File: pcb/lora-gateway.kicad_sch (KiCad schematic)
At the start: 22 parts, among them J1 USB_B_Micro, J2 Conn_01x06, J3 Conn_01x06, J4 Conn_Coaxial, J5 AVR-JTAG-10, J6 AVR-ISP-6, SW1 SW_Push, U1 RFM95W-868S2, U2 ATmega2560-16A, U3 LM1117-3.3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

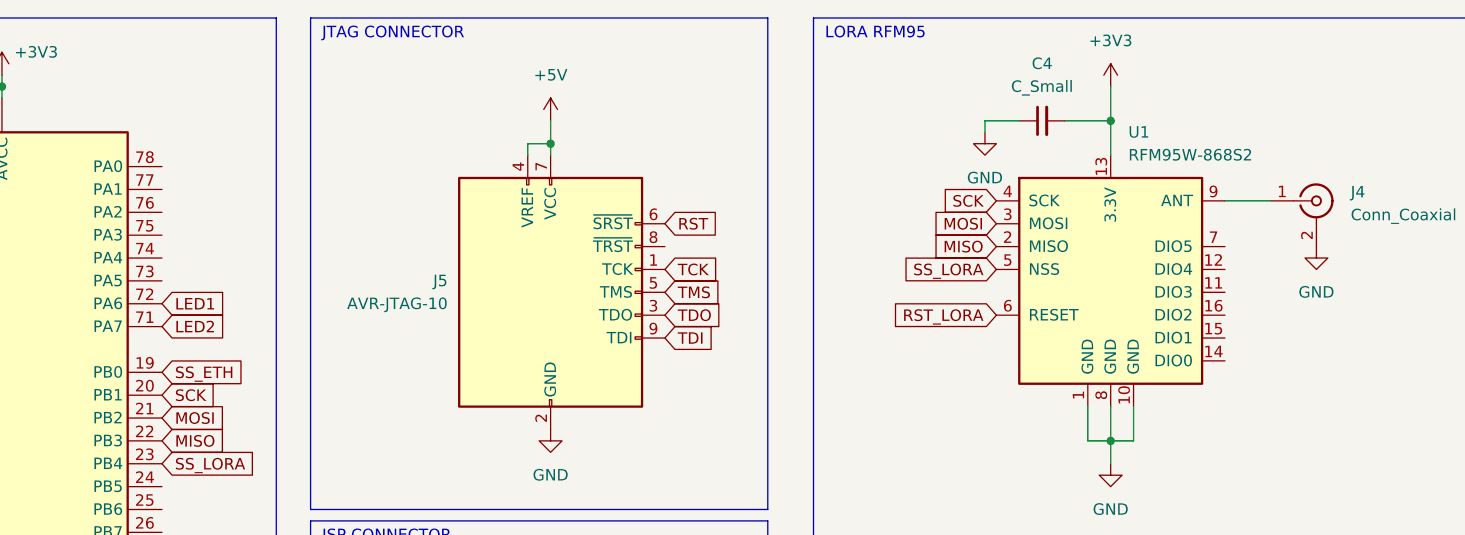
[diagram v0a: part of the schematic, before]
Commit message: add rfm95 wiring
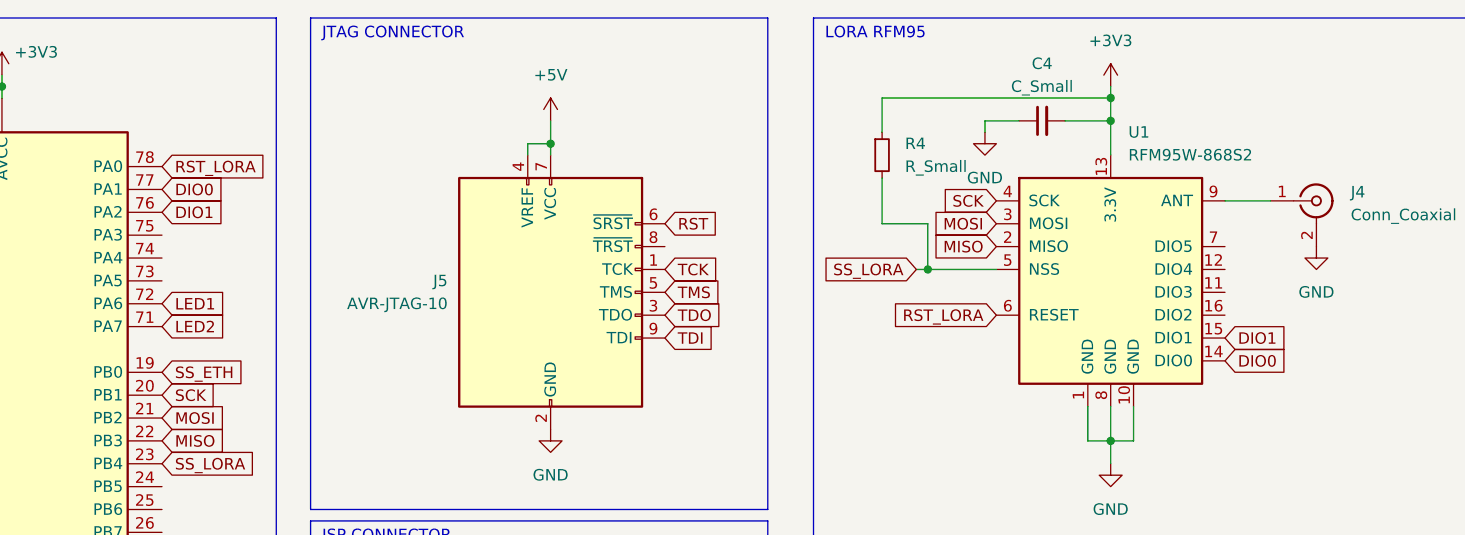
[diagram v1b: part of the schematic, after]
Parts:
- added R4: R_Small, Resistor_SMD:R_0603_1608Metric, symbol Device:R_Small
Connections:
- net +3V3: now also R4.1
- net RST_LORA: now also U2.78 (PA0)
- net SS_LORA: now also R4.2
- net DIO1: now reaches U2.76 (PA2)
- net DIO1: now also U1.15 (DIO1)
- net DIO0: now reaches U2.77 (PA1)
- net DIO0: now also U1.14 (DIO0)
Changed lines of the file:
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@@
   (junction (at 41.91 74.93) (diameter 0) (color 0 0 0 0)
   )
+  (junction (at 199.39 43.18) (diameter 0) (color 0 0 0 0)
+  )
   (junction (at 219.71 26.67) (diameter 0) (color 0 0 0 0)
   )
@@
   (junction (at 45.72 36.83) (diameter 0) (color 0 0 0 0)
   )
+  (junction (at 219.71 24.13) (diameter 0) (color 0 0 0 0)
+  )
   (junction (at 66.04 44.45) (diameter 0) (color 0 0 0 0)
   )
@@
     (stroke (width 0) (type default))
   )
+  (wire (pts (xy 194.31 33.02) (xy 194.31 38.1))
+    (stroke (width 0) (type default))
+  )
   (wire (pts (xy 219.71 96.52) (xy 220.98 96.52))
     (stroke (width 0) (type default))
@@
     (stroke (width 0) (type default))
   )
+  (wire (pts (xy 194.31 24.13) (xy 219.71 24.13))
+    (stroke (width 0) (type default))
+  )
   (wire (pts (xy 219.71 62.23) (xy 219.71 64.77))
     (stroke (width 0) (type default))
@@
     (stroke (width 0) (type default))
   )
+  (wire (pts (xy 194.31 27.94) (xy 194.31 24.13))
+    (stroke (width 0) (type default))
+  )
   (polyline (pts (xy 67.31 52.07) (xy 67.31 182.88))
     (stroke (width 0) (type default))
@@
     (stroke (width 0) (type default))
   )
+  (wire (pts (xy 219.71 24.13) (xy 219.71 26.67))
+    (stroke (width 0) (type default))
+  )
   (wire (pts (xy 219.71 58.42) (xy 219.71 62.23))
     (stroke (width 0) (type default))
@@
     (stroke (width 0) (type default))
   )
+  (wire (pts (xy 199.39 43.18) (xy 207.01 43.18))
+    (stroke (width 0) (type default))
+  )
   (wire (pts (xy 71.12 31.75) (xy 73.66 31.75))
     (stroke (width 0) (type default))
@@
     (stroke (width 0) (type default))
   )
+  (wire (pts (xy 199.39 38.1) (xy 199.39 43.18))
+    (stroke (width 0) (type default))
+  )
   (wire (pts (xy 46.99 74.93) (xy 41.91 74.93))
     (stroke (width 0) (type default))
@@
     (stroke (width 0) (type default))
   )
+  (wire (pts (xy 194.31 38.1) (xy 199.39 38.1))
+    (stroke (width 0) (type default))
+  )
   (polyline (pts (xy 15.24 52.07) (xy 40.64 52.07))
     (stroke (width 0) (type default))
@@
     (stroke (width 0) (type default))
   )
-  (wire (pts (xy 219.71 22.86) (xy 219.71 26.67))
+  (wire (pts (xy 219.71 22.86) (xy 219.71 24.13))
     (stroke (width 0) (type default))
   )
@@
   )
   (polyline (pts (xy 181.61 15.24) (xy 130.81 15.24))
+    (stroke (width 0) (type default))
+  )
+  (wire (pts (xy 198.12 43.18) (xy 199.39 43.18))
     (stroke (width 0) (type default))
   )
@@
   (text "JTAG CONNECTOR" (at 132.08 17.78 0)
     (effects (font (size 1.27 1.27)) (justify left bottom))
+  )
+  (global_label "DIO0" (shape input) (at 114.3 34.29 0) (fields_autoplaced)
+    (effects (font (size 1.27 1.27)) (justify left))
+    (property "Intersheetrefs" "${INTERSHEET_REFS}" (at 121.7 34.29 0)
+      (effects (font (size 1.27 1.27)) (justify left) hide)
+    )
   )
   (global_label "RST_LORA" (shape input) (at 207.01 48.26 180) (fields_autoplaced)
@@
     )
   )
+  (global_label "DIO1" (shape input) (at 114.3 36.83 0) (fields_autoplaced)
+    (effects (font (size 1.27 1.27)) (justify left))
+    (property "Intersheetrefs" "${INTERSHEET_REFS}" (at 121.7 36.83 0)
+      (effects (font (size 1.27 1.27)) (justify left) hide)
+    )
+  )
   (global_label "TMS" (shape input) (at 170.18 45.72 0) (fields_autoplaced)
     (effects (font (size 1.27 1.27)) (justify left))
@@
     (effects (font (size 1.27 1.27)) (justify left))
     (property "Intersheetrefs" "${INTERSHEET_REFS}" (at 178.1847 92.71 0)
+      (effects (font (size 1.27 1.27)) (justify left) hide)
+    )
+  )
+  (global_label "DIO1" (shape input) (at 232.41 50.8 0) (fields_autoplaced)
+    (effects (font (size 1.27 1.27)) (justify left))
+    (property "Intersheetrefs" "${INTERSHEET_REFS}" (at 239.81 50.8 0)
+      (effects (font (size 1.27 1.27)) (justify left) hide)
+    )
+  )
+  (global_label "RST_LORA" (shape input) (at 114.3 31.75 0) (fields_autoplaced)
+    (effects (font (size 1.27 1.27)) (justify left))
+    (property "Intersheetrefs" "${INTERSHEET_REFS}" (at 126.4171 31.75 0)
       (effects (font (size 1.27 1.27)) (justify left) hide)
     )
@@
     )
   )
-  (global_label "SS_LORA" (shape input) (at 207.01 43.18 180) (fields_autoplaced)
+  (global_label "SS_LORA" (shape input) (at 198.12 43.18 180) (fields_autoplaced)
     (effects (font (size 1.27 1.27)) (justify right))
-    (property "Intersheetrefs" "${INTERSHEET_REFS}" (at 195.921 43.18 0)
+    (property "Intersheetrefs" "${INTERSHEET_REFS}" (at 187.031 43.18 0)
       (effects (font (size 1.27 1.27)) (justify right) hide)
     )
@@
     (property "Intersheetrefs" "${INTERSHEET_REFS}" (at 213.8219 106.68 0)
       (effects (font (size 1.27 1.27)) (justify right) hide)
+    )
+  )
+  (global_label "DIO0" (shape input) (at 232.41 53.34 0) (fields_autoplaced)
+    (effects (font (size 1.27 1.27)) (justify left))
+    (property "Intersheetrefs" "${INTERSHEET_REFS}" (at 239.81 53.34 0)
+      (effects (font (size 1.27 1.27)) (justify left) hide)
     )
   )
@@
         )
       )
+    )
+  )
+  (symbol (lib_id "Device:R_Small") (at 194.31 30.48 0) (unit 1)
+    (in_bom yes) (on_board yes) (dnp no) (fields_autoplaced)
+    (property "Reference" "R4" (at 196.85 29.21 0)
+      (effects (font (size 1.27 1.27)) (justify left))
+    )
+    (property "Value" "R_Small" (at 196.85 31.75 0)
+      (effects (font (size 1.27 1.27)) (justify left))
+    )
+    (property "Footprint" "Resistor_SMD:R_0603_1608Metric" (at 194.31 30.48 0)
+      (effects (font (size 1.27 1.27)) hide)
+    )
+    (property "Datasheet" "~" (at 194.31 30.48 0)
+      (effects (font (size 1.27 1.27)) hide)
+    )
+    (pin "1")
+    (pin "2")
+    (instances
+      (project "lora-gateway"
+        (path "/5fd0eb65-7f10-4bbb-b642-b528dcb1ea0e"
+          (reference "R4") (unit 1)
+        )
+      )

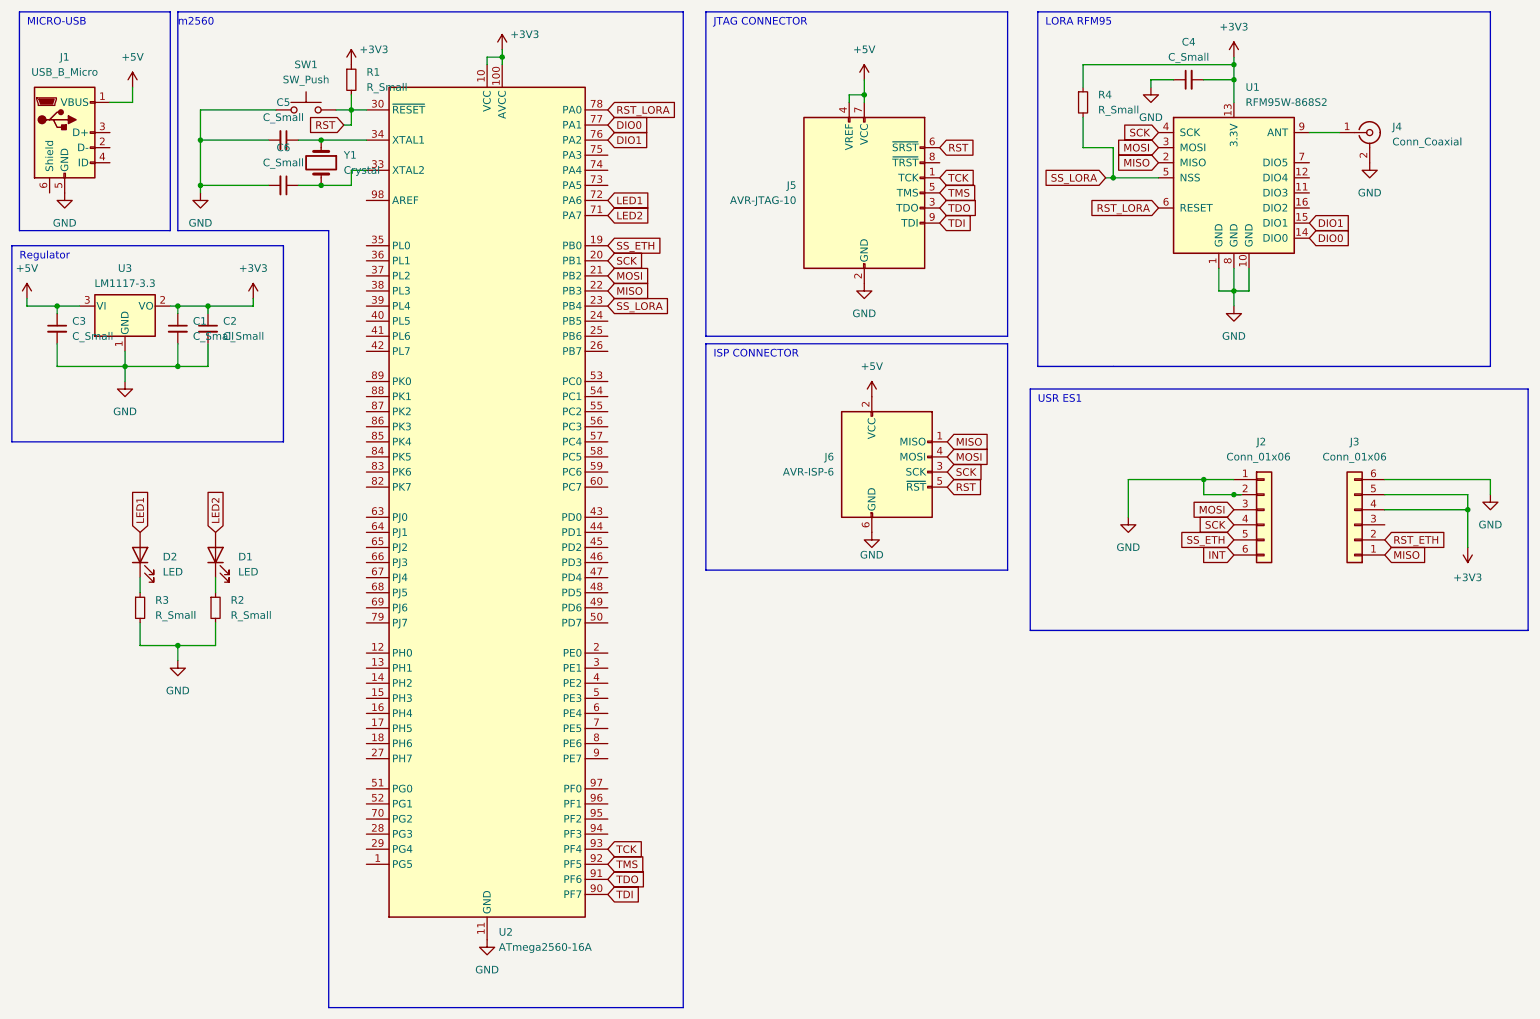
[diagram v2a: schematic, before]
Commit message: change DIO0 & DIO1 to interrupt pin
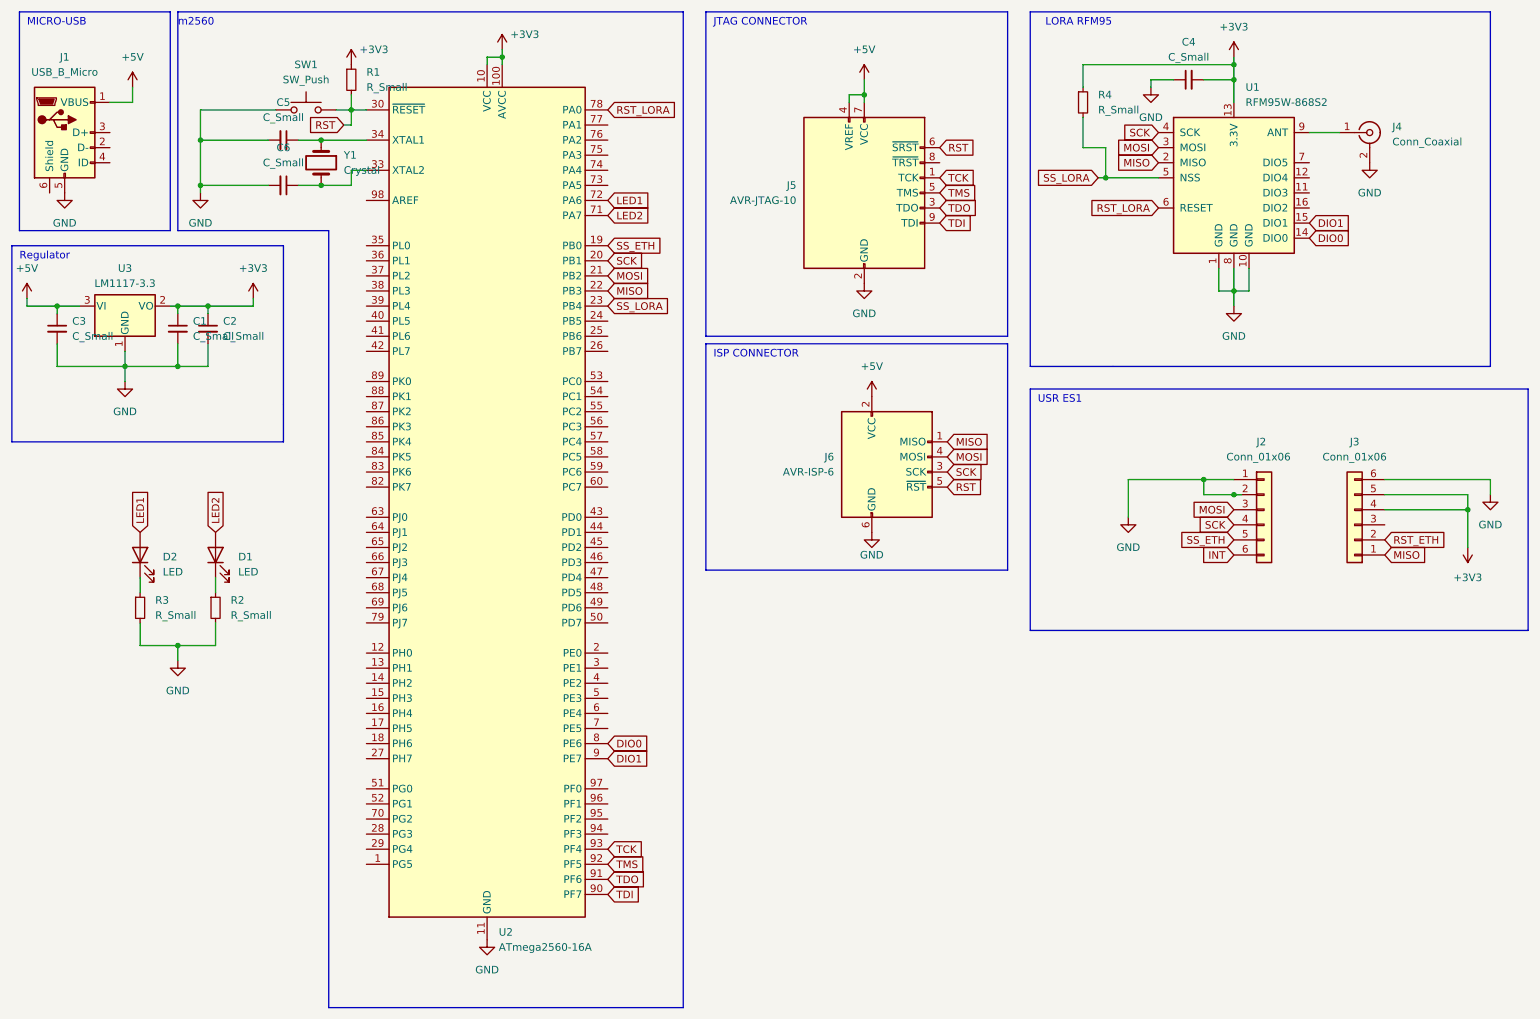
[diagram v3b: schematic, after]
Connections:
- net DIO0: now also U2.8 (PE6); no longer U2.77 (PA1)
- net DIO1: now also U2.9 (PE7); no longer U2.76 (PA2)
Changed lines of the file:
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@@
   (junction (at 41.91 74.93) (diameter 0) (color 0 0 0 0)
   )
-  (junction (at 199.39 43.18) (diameter 0) (color 0 0 0 0)
-  )
   (junction (at 219.71 26.67) (diameter 0) (color 0 0 0 0)
   )
@@
   (junction (at 96.52 22.86) (diameter 0) (color 0 0 0 0)
   )
+  (junction (at 198.12 43.18) (diameter 0) (color 0 0 0 0)
+  )
   (junction (at 259.08 99.06) (diameter 0) (color 0 0 0 0)
   )
@@
     (stroke (width 0) (type default))
   )
-  (polyline (pts (xy 186.69 74.93) (xy 199.39 74.93))
+  (polyline (pts (xy 185.42 74.93) (xy 199.39 74.93))
+    (stroke (width 0) (type default))
+  )
+  (wire (pts (xy 198.12 43.18) (xy 207.01 43.18))
     (stroke (width 0) (type default))
   )
@@
     (stroke (width 0) (type default))
   )
-  (wire (pts (xy 199.39 43.18) (xy 207.01 43.18))
-    (stroke (width 0) (type default))
-  )
   (wire (pts (xy 71.12 31.75) (xy 73.66 31.75))
     (stroke (width 0) (type default))
@@
     (stroke (width 0) (type default))
   )
-  (wire (pts (xy 199.39 38.1) (xy 199.39 43.18))
+  (wire (pts (xy 198.12 38.1) (xy 198.12 43.18))
     (stroke (width 0) (type default))
   )
@@
     (stroke (width 0) (type default))
   )
-  (wire (pts (xy 194.31 38.1) (xy 199.39 38.1))
+  (wire (pts (xy 194.31 38.1) (xy 198.12 38.1))
     (stroke (width 0) (type default))
   )
@@
     (stroke (width 0) (type default))
   )
-  (polyline (pts (xy 262.89 15.24) (xy 186.69 15.24))
+  (polyline (pts (xy 262.89 15.24) (xy 185.42 15.24))
     (stroke (width 0) (type default))
   )
@@
     (stroke (width 0) (type default))
   )
-  (wire (pts (xy 198.12 43.18) (xy 199.39 43.18))
+  (wire (pts (xy 196.85 43.18) (xy 198.12 43.18))
     (stroke (width 0) (type default))
   )
@@
     (stroke (width 0) (type default))
   )
-  (polyline (pts (xy 186.69 15.24) (xy 186.69 74.93))
+  (polyline (pts (xy 185.42 15.24) (xy 185.42 74.93))
     (stroke (width 0) (type default))
   )
@@
     (effects (font (size 1.27 1.27)) (justify left bottom))
   )
-  (global_label "DIO0" (shape input) (at 114.3 34.29 0) (fields_autoplaced)
-    (effects (font (size 1.27 1.27)) (justify left))
-    (property "Intersheetrefs" "${INTERSHEET_REFS}" (at 121.7 34.29 0)
-      (effects (font (size 1.27 1.27)) (justify left) hide)
-    )
-  )
   (global_label "RST_LORA" (shape input) (at 207.01 48.26 180) (fields_autoplaced)
     (effects (font (size 1.27 1.27)) (justify right))
@@
     )
   )
-  (global_label "DIO1" (shape input) (at 114.3 36.83 0) (fields_autoplaced)
-    (effects (font (size 1.27 1.27)) (justify left))
-    (property "Intersheetrefs" "${INTERSHEET_REFS}" (at 121.7 36.83 0)
-      (effects (font (size 1.27 1.27)) (justify left) hide)
-    )
-  )
   (global_label "TMS" (shape input) (at 170.18 45.72 0) (fields_autoplaced)
     (effects (font (size 1.27 1.27)) (justify left))
@@
     )
   )
+  (global_label "DIO0" (shape input) (at 114.3 138.43 0) (fields_autoplaced)
+    (effects (font (size 1.27 1.27)) (justify left))
+    (property "Intersheetrefs" "${INTERSHEET_REFS}" (at 121.7 138.43 0)
+      (effects (font (size 1.27 1.27)) (justify left) hide)
+    )
+  )
   (global_label "SCK" (shape input) (at 171.45 92.71 0) (fields_autoplaced)
     (effects (font (size 1.27 1.27)) (justify left))
@@
     )
   )
-  (global_label "SS_LORA" (shape input) (at 198.12 43.18 180) (fields_autoplaced)
-    (effects (font (size 1.27 1.27)) (justify right))
-    (property "Intersheetrefs" "${INTERSHEET_REFS}" (at 187.031 43.18 0)
+  (global_label "SS_LORA" (shape input) (at 196.85 43.18 180) (fields_autoplaced)
+    (effects (font (size 1.27 1.27)) (justify right))
+    (property "Intersheetrefs" "${INTERSHEET_REFS}" (at 185.761 43.18 0)
       (effects (font (size 1.27 1.27)) (justify right) hide)
     )
@@
       (effects (font (size 1.27 1.27)) (justify left) hide)
     )
+  )
+  (global_label "DIO1" (shape input) (at 114.3 140.97 0) (fields_autoplaced)
+    (effects (font (size 1.27 1.27)) (justify left))
+    (property "Intersheetrefs" "${INTERSHEET_REFS}" (at 121.7 140.97 0)
+      (effects (font (size 1.27 1.27)) (justify left) hide)
+    )
